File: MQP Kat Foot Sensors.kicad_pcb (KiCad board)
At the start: 2 copper layers, 48 x 48 mm, 33 parts, among them IC1 BMP280, IC2 BMP280, IC3 BMP280, IC4 BMP280, IC5 BMP280, IC6 BMP280, IC7 BMP280, J1 Conn_01x06_Male, J2 Conn_01x04_Male, U1 STM32L432KBUx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

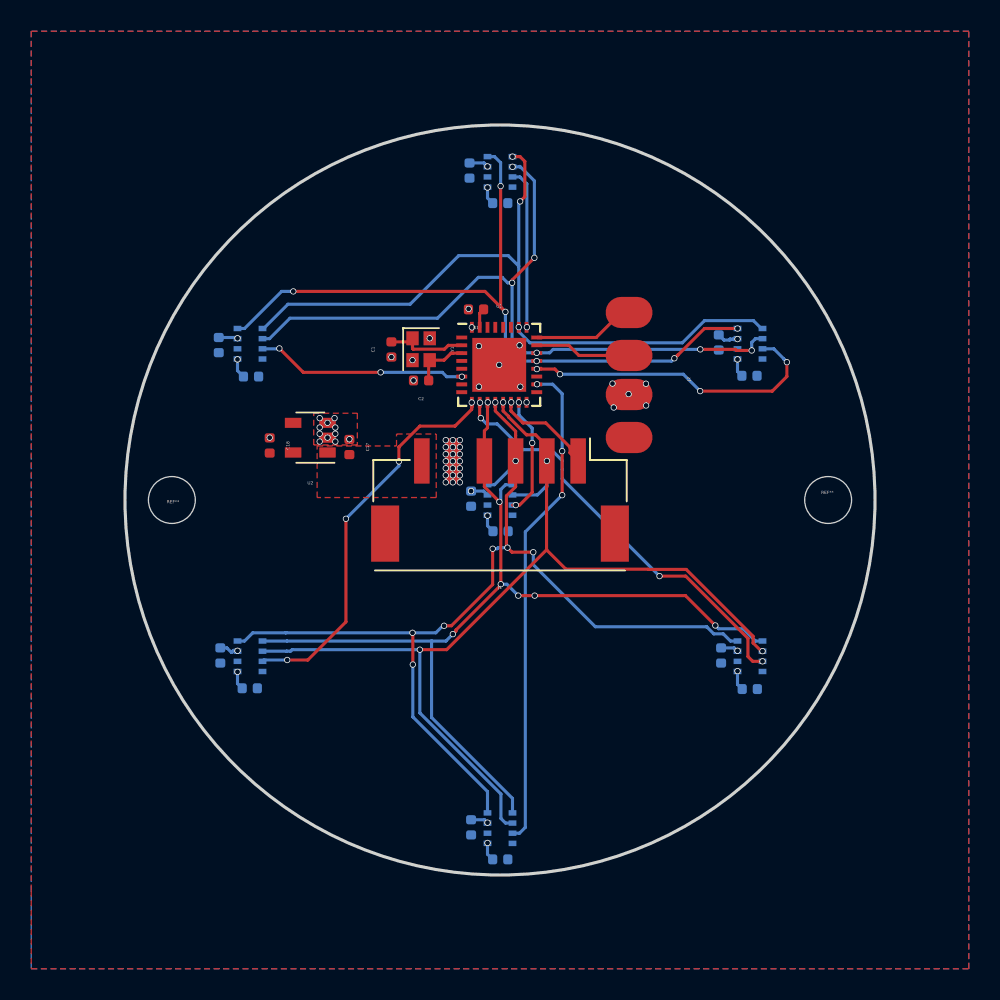
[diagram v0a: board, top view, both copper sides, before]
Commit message: updated pinout
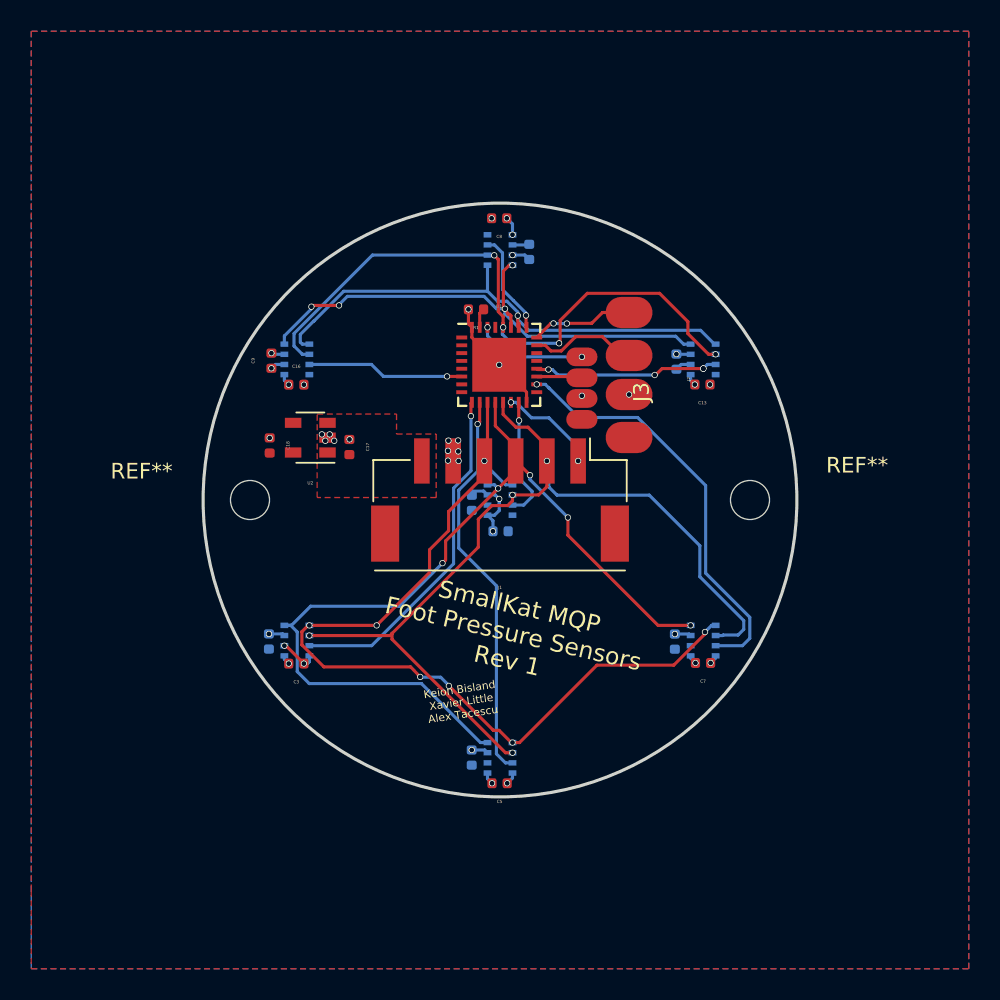
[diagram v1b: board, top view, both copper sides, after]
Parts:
- removed C1, C2: 10PF, Capacitor_SMD:C_0402_1005Metric
- removed the REF** at (-21.0, 0.00)
- removed the REF** at (21.0, 0.00)
- removed Y1: Crystal_GND24, Crystal:Crystal_SMD_2016-4Pin_2.0x1.6mm
- added J3: Conn_01x04_Male, pads1x4:1x4Pads, F.Cu at (5.24, -7.16)
- added REF**: MountingHole_2.5mm, MountingHole:MountingHole_2.5mm, F.Cu at (16.0, 0.00)
- added REF**: MountingHole_2.5mm, MountingHole:MountingHole_2.5mm, F.Cu at (-16.0, 0.00)
- C13, C16, C3, C5, C7, C8, C9: moved to F.Cu
- moved C10 6.46 mm to (1.87, -15.9), turned to 90 degrees
- moved IC2 5.00 mm to (0.00, -16.0), turned to 180 degrees
- moved C5 4.87 mm to (-0.03, 18.1)
- moved IC3 4.50 mm to (0.00, 16.5)
- moved C6 4.47 mm to (-1.81, 16.5)
- moved C9 3.52 mm to (-14.6, -8.91)
- moved C7 3.42 mm to (13.0, 10.4)
- moved C3 3.37 mm to (-13.0, 10.5)
- moved C4 3.24 mm to (-14.8, 9.05)
- moved IC1 3.16 mm to (-13.0, -9.00)
- moved IC5 3.16 mm to (13.0, -9.00)
- moved IC6 3.16 mm to (-13.0, 9.00)
- moved IC7 3.16 mm to (13.0, 9.00)
- moved C11 3.09 mm to (11.2, 9.06)
- moved C13 3.06 mm to (13.0, -7.39)
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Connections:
- IC3 pad 2: CS5 -> CS6
- IC7 pad 2: CS6 -> CS5
- U1 pad 19: (no net) -> TX
- U1 pad 2: Net-(C1-Pad2) -> (no net)
- U1 pad 21: MISO2 -> (no net)
- U1 pad 22: MOSI2 -> (no net)
- U1 pad 27: (no net) -> MISO2
- U1 pad 28: (no net) -> MOSI2
- U1 pad 3: Net-(C2-Pad1) -> (no net)
- U1 pad 30: (no net) -> RX
- U2 pad 3: GND -> +BATT
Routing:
- net GND: track 0.00 -> 14.4 mm, vias 50 -> 24
- net SCK2: track 47.3 -> 33.0 mm, vias 3 -> 1
- net MISO2: track 47.8 -> 33.8 mm, vias 6 -> 4
- net CS4: track 19.8 -> 11.9 mm
- net MOSI2: track 47.7 -> 40.3 mm, vias 6 -> 4
- net RX: track 0.00 -> 7.15 mm, vias 0 -> 2
- net MOSI: track 66.4 -> 59.9 mm
- net MISO: track 64.9 -> 59.0 mm, vias 8 -> 5
- net Net-(C1-Pad2): track 5.37 -> 0.00 mm
- net CS5: track 31.6 -> 26.8 mm, vias 3 -> 1
- net SCK: track 62.1 -> 57.8 mm
- net CS3: track 10.3 -> 6.57 mm
- net Net-(C2-Pad1): track 3.56 -> 0.00 mm
- net CS1: track 13.5 -> 10.1 mm, vias 3 -> 1
- net TX: track 0.00 -> 2.93 mm
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- removed copper zone on F.Cu, net GND
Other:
- board size 48 x 48 mm -> 38 x 38 mm
- board text added: "Keion Bisland Xavier Little Alex Tacescu"
- board text added: "SmallKat MQP Foot Pressure Sensors Rev 1"
